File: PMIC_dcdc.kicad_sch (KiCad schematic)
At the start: 21 parts, among them U5 RK809-2

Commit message: updated foorprints
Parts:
- L1, L2, L3, L4: value 470nH 0.035ohm -> 470nH 4.53A 0.035ohm; footprint (none) -> Inductor_SMD:L_1008_2520Metric; LCSC (none) -> C88530; Model (none) -> VLS252010HBX-R47M-1; Vendor (none) -> TDK
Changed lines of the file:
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@@
       (effects (font (size 1.27 1.27)))
     )
-    (property "Value" "470nH 0.035ohm" (at 193.04 96.52 90)
-      (effects (font (size 1.27 1.27)))
-    )
-    (property "Footprint" "" (at 193.04 93.98 0)
+    (property "Value" "470nH 4.53A 0.035ohm" (at 193.04 96.52 90)
+      (effects (font (size 1.27 1.27)))
+    )
+    (property "Footprint" "Inductor_SMD:L_1008_2520Metric" (at 193.04 93.98 0)
       (effects (font (size 1.27 1.27)) hide)
     )
     (property "Datasheet" "~" (at 193.04 93.98 0)
+      (effects (font (size 1.27 1.27)) hide)
+    )
+    (property "Description" "电感值: 470nH 精度: ±20% 额定电流: 3.32A 饱和电流(Isat): 4.53A 直流电阻(DCR): 35mΩ Q值: - 自谐振频率: - 车" (at 193.04 93.98 0)
+      (effects (font (size 1.27 1.27)) hide)
+    )
+    (property "LCSC" "C88530" (at 193.04 93.98 0)
+      (effects (font (size 1.27 1.27)) hide)
+    )
+    (property "Model" "VLS252010HBX-R47M-1" (at 193.04 93.98 0)
+      (effects (font (size 1.27 1.27)) hide)
+    )
+    (property "Vendor" "TDK" (at 193.04 93.98 0)
       (effects (font (size 1.27 1.27)) hide)
     )
@@
       (effects (font (size 1.27 1.27)))
     )
-    (property "Value" "470nH 0.035ohm" (at 194.31 69.85 90)
-      (effects (font (size 1.27 1.27)))
-    )
-    (property "Footprint" "" (at 194.31 67.31 0)
+    (property "Value" "470nH 4.53A 0.035ohm" (at 194.31 69.85 90)
+      (effects (font (size 1.27 1.27)))
+    )
+    (property "Footprint" "Inductor_SMD:L_1008_2520Metric" (at 194.31 67.31 0)
       (effects (font (size 1.27 1.27)) hide)
     )
     (property "Datasheet" "~" (at 194.31 67.31 0)
+      (effects (font (size 1.27 1.27)) hide)
+    )
+    (property "Description" "电感值: 470nH 精度: ±20% 额定电流: 3.32A 饱和电流(Isat): 4.53A 直流电阻(DCR): 35mΩ Q值: - 自谐振频率: - 车" (at 194.31 67.31 0)
+      (effects (font (size 1.27 1.27)) hide)
+    )
+    (property "LCSC" "C88530" (at 194.31 67.31 0)
+      (effects (font (size 1.27 1.27)) hide)
+    )
+    (property "Model" "VLS252010HBX-R47M-1" (at 194.31 67.31 0)
+      (effects (font (size 1.27 1.27)) hide)
+    )
+    (property "Vendor" "TDK" (at 194.31 67.31 0)
       (effects (font (size 1.27 1.27)) hide)
     )
@@
       (effects (font (size 1.27 1.27)))
     )
-    (property "Value" "470nH 0.035ohm" (at 102.87 69.85 90)
-      (effects (font (size 1.27 1.27)))
-    )
-    (property "Footprint" "" (at 102.87 67.31 0)
+    (property "Value" "470nH 4.53A 0.035ohm" (at 102.87 69.85 90)
+      (effects (font (size 1.27 1.27)))
+    )
+    (property "Footprint" "Inductor_SMD:L_1008_2520Metric" (at 102.87 67.31 0)
       (effects (font (size 1.27 1.27)) hide)
     )
@@
       (effects (font (size 1.27 1.27)) hide)
     )
+    (property "Description" "电感值: 470nH 精度: ±20% 额定电流: 3.32A 饱和电流(Isat): 4.53A 直流电阻(DCR): 35mΩ Q值: - 自谐振频率: - 车" (at 102.87 67.31 0)
+      (effects (font (size 1.27 1.27)) hide)
+    )
+    (property "LCSC" "C88530" (at 102.87 67.31 0)
+      (effects (font (size 1.27 1.27)) hide)
+    )
+    (property "Model" "VLS252010HBX-R47M-1" (at 102.87 67.31 0)
+      (effects (font (size 1.27 1.27)) hide)
+    )
+    (property "Vendor" "TDK" (at 102.87 67.31 0)
+      (effects (font (size 1.27 1.27)) hide)
+    )
     (pin "1")
     (pin "2")
@@
       (effects (font (size 1.27 1.27)))
     )
-    (property "Value" "470nH 0.035ohm" (at 104.14 107.95 90)
-      (effects (font (size 1.27 1.27)))
-    )
-    (property "Footprint" "" (at 104.14 105.41 0)
+    (property "Value" "470nH 4.53A 0.035ohm" (at 104.14 107.95 90)
+      (effects (font (size 1.27 1.27)))
+    )
+    (property "Footprint" "Inductor_SMD:L_1008_2520Metric" (at 104.14 105.41 0)
       (effects (font (size 1.27 1.27)) hide)
     )
@@
       (effects (font (size 1.27 1.27)) hide)
     )
+    (property "Description" "电感值: 470nH 精度: ±20% 额定电流: 3.32A 饱和电流(Isat): 4.53A 直流电阻(DCR): 35mΩ Q值: - 自谐振频率: - 车" (at 104.14 105.41 0)
+      (effects (font (size 1.27 1.27)) hide)
+    )
+    (property "LCSC" "C88530" (at 104.14 105.41 0)
+      (effects (font (size 1.27 1.27)) hide)
+    )
+    (property "Model" "VLS252010HBX-R47M-1" (at 104.14 105.41 0)
+      (effects (font (size 1.27 1.27)) hide)
+    )
+    (property "Vendor" "TDK" (at 104.14 105.41 0)
+      (effects (font (size 1.27 1.27)) hide)
+    )

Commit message: fix some ERCs
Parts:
- renumbered C50 to C64, C51 to C65, C52 to C66, C53 to C67, C54 to C68, C55 to C69, C56 to C70, C57 to C71, C58 to C72, C59 to C73, C60 to C74, C61 to C75, R47 to R43, R48 to R44, R49 to R45, R50 to R46, U5 to U4
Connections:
- net VDD_DDR renamed VCC_DDR
- net VDD_NPU_VEPU renamed VDD_NPU

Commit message: added VDD Logic
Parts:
- R43, R44: LCSC (none) -> C25138; Model (none) -> 0402WGJ0101TCE; Vendor (none) -> UNI-ROYAL(厚声)
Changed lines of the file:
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@@
+      (effects (font (size 1.27 1.27)) hide)
+    )
+    (property "Description" "电阻类型: 厚膜电阻 阻值: 100Ω 精度: ±5% 功率: 1/16W 温度系数: ±100ppm/℃ 最大工作电压: 50V 工作温度" (at 102.87 76.2 0)
+      (effects (font (size 1.27 1.27)) hide)
+    )
+    (property "LCSC" "C25138" (at 102.87 76.2 0)
+      (effects (font (size 1.27 1.27)) hide)
+    )
+    (property "Model" "0402WGJ0101TCE" (at 102.87 76.2 0)
+      (effects (font (size 1.27 1.27)) hide)
+    )
+    (property "Vendor" "UNI-ROYAL(厚声)" (at 102.87 76.2 0)
       (effects (font (size 1.27 1.27)) hide)
     )
@@
       (effects (font (size 1.27 1.27)) hide)
     )
+    (property "Description" "电阻类型: 厚膜电阻 阻值: 100Ω 精度: ±5% 功率: 1/16W 温度系数: ±100ppm/℃ 最大工作电压: 50V 工作温度" (at 104.14 114.3 0)
+      (effects (font (size 1.27 1.27)) hide)
+    )
+    (property "LCSC" "C25138" (at 104.14 114.3 0)
+      (effects (font (size 1.27 1.27)) hide)
+    )
+    (property "Model" "0402WGJ0101TCE" (at 104.14 114.3 0)
+      (effects (font (size 1.27 1.27)) hide)
+    )
+    (property "Vendor" "UNI-ROYAL(厚声)" (at 104.14 114.3 0)
+      (effects (font (size 1.27 1.27)) hide)
+    )

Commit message: updated for ERC
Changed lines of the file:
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@@
-    (stroke (width 0) (type default))
-  )
-  (wire (pts (xy 232.41 113.03) (xy 232.41 114.3))
     (stroke (width 0) (type default))
   )
@@
         )
       )
-    )
-  )
-  (symbol (lib_id "power:PWR_FLAG") (at 232.41 113.03 0) (unit 1)
-    (in_bom yes) (on_board yes) (dnp no) (fields_autoplaced)
-    (property "Reference" "#FLG011" (at 232.41 111.125 0)
-      (effects (font (size 1.27 1.27)) hide)
-    )
-    (property "Value" "PWR_FLAG" (at 232.41 109.5281 0)
-      (effects (font (size 1.27 1.27)))
-    )
-    (property "Footprint" "" (at 232.41 113.03 0)
-      (effects (font (size 1.27 1.27)) hide)
-    )
-    (property "Datasheet" "~" (at 232.41 113.03 0)
-      (effects (font (size 1.27 1.27)) hide)
-    )
-    (pin "1")
-    (instances
-      (project "leaf"
-        (path "/e3b58043-16a3-43c8-9fad-9c9784eebfa4/cc9fb3ac-19c3-47a8-ba7d-678b4d514ff0/46e9a7bf-8506-4399-90d8-57d007223126/2d95e8c5-bd08-40b5-b7b2-fac89748aabf"
-          (reference "#FLG011") (unit 1)
-        )
-      )

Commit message: added OSC, updated annotations
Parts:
- renumbered C64 to C14001, C65 to C14002, C66 to C14003, C67 to C14004, C68 to C14005, C69 to C14006, C70 to C14007, C71 to C14008, C72 to C14009, C73 to C14010, C74 to C14011, C75 to C14012, L1 to L14001, L2 to L14002, L3 to L14003, L4 to L14004, R43 to R14001, R44 to R14002, R45 to R14003, R46 to R14004, U4 to U13001

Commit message: move DDR power decoupling capacitors into DDR4 Sheet
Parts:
- renumbered C14001 to C68, C14002 to C69, C14003 to C70, C14004 to C71, C14005 to C72, C14006 to C73, C14007 to C74, C14008 to C75, C14009 to C76, C14010 to C77, C14011 to C78, C14012 to C79, L14001 to L2, L14002 to L3, L14003 to L4, L14004 to L5, R14001 to R43, R14002 to R44, R14003 to R45, R14004 to R46, U13001 to U5

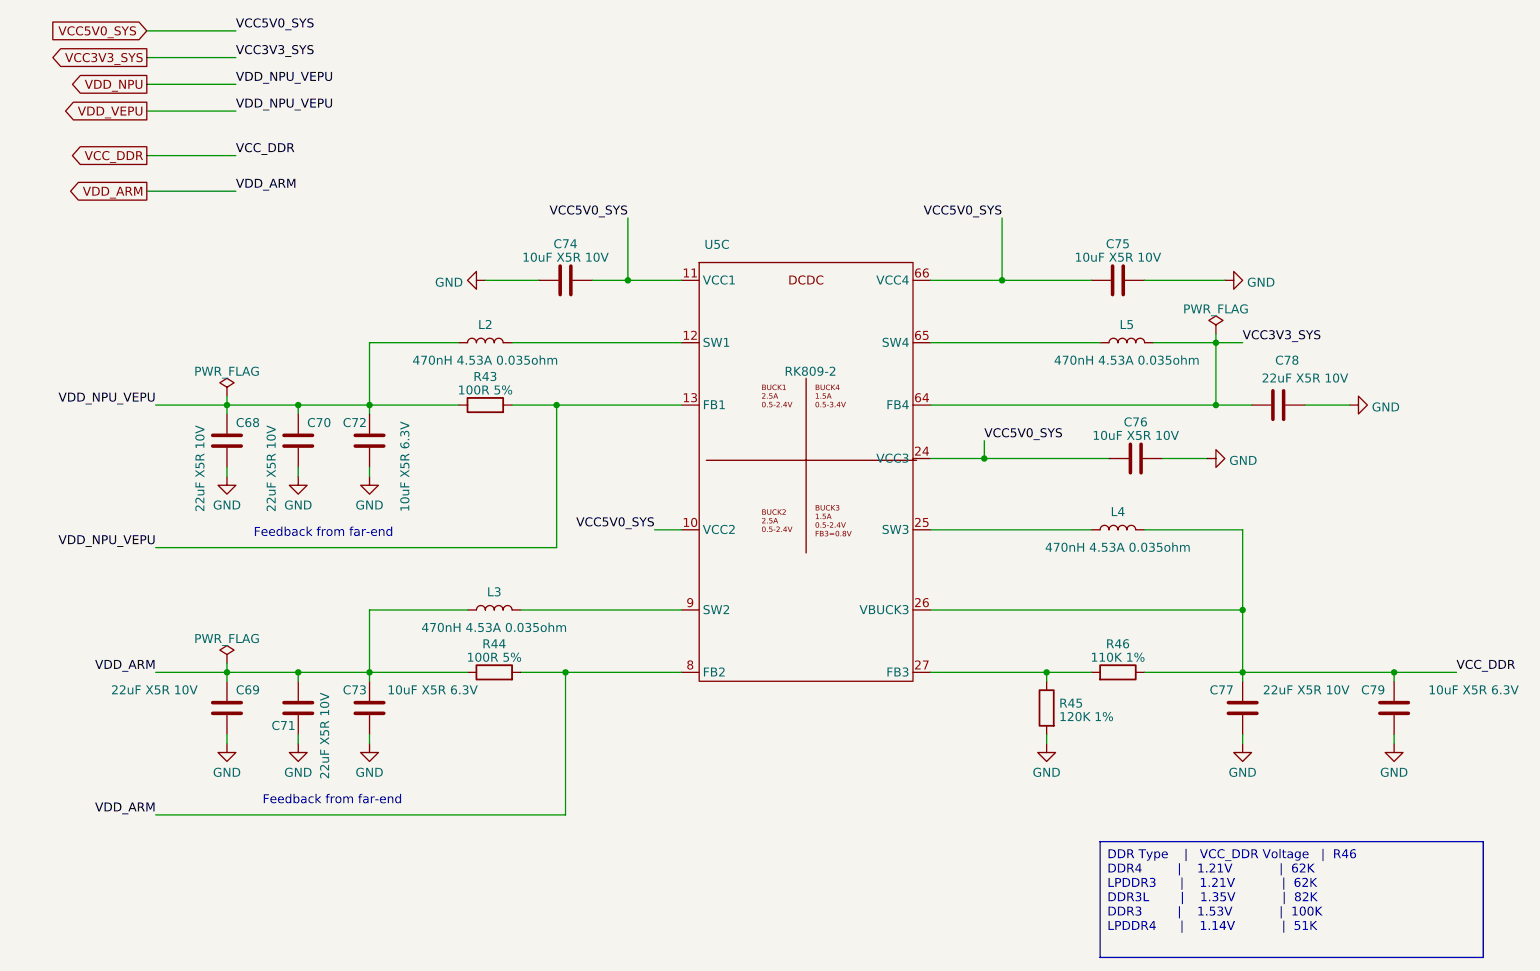
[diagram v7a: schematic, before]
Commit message: resort all symbols
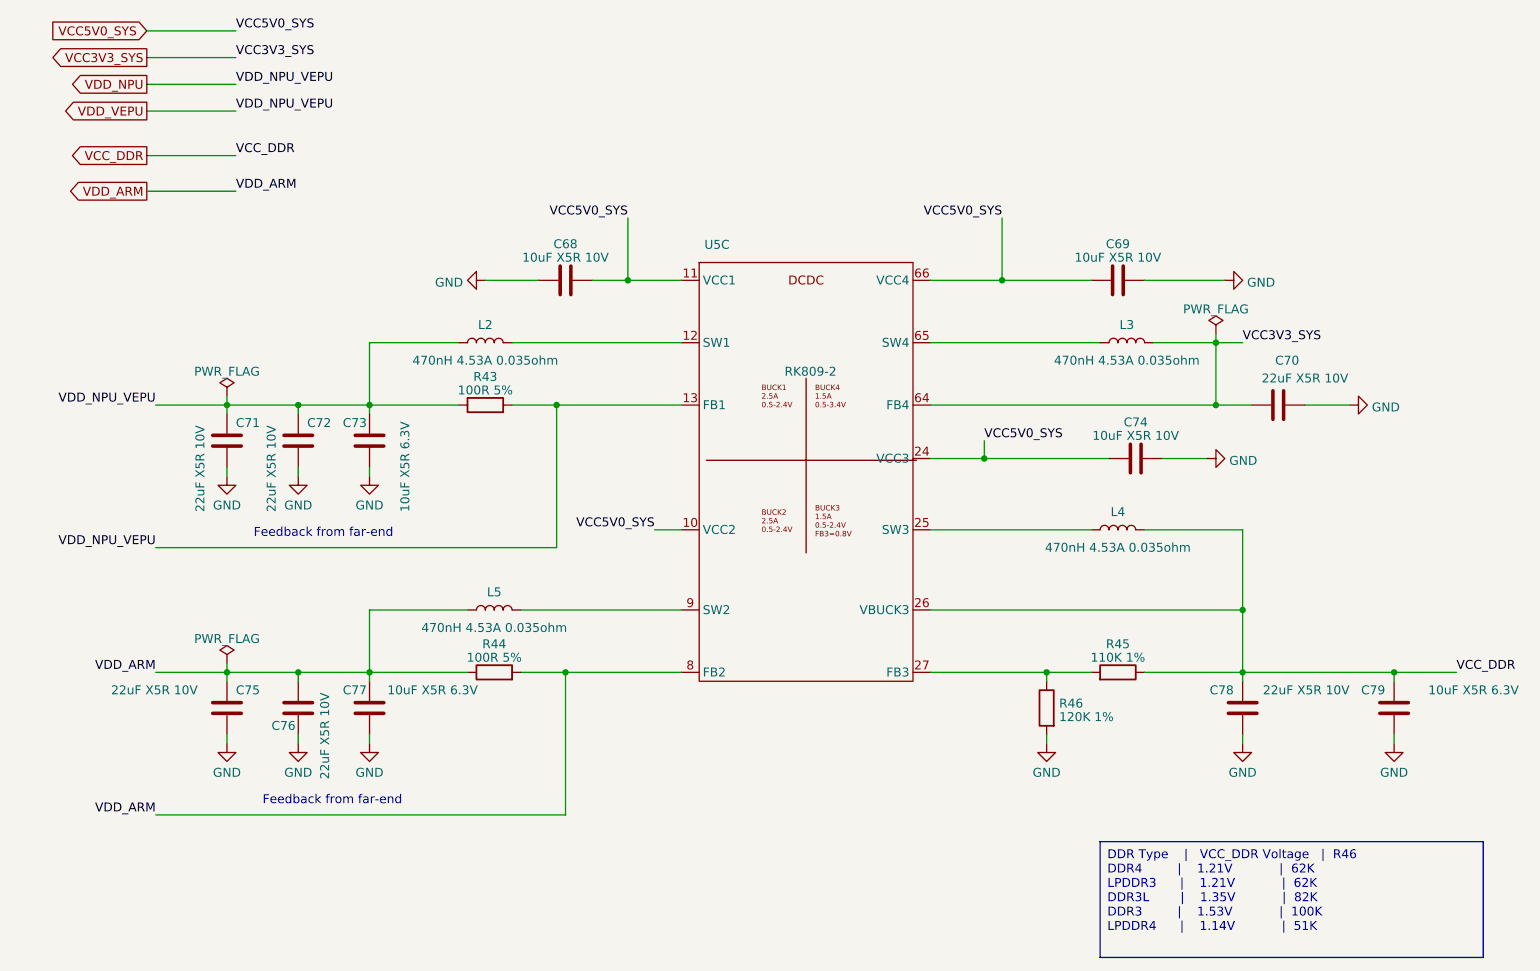
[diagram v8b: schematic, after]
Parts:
- renumbered C74 to C68, C75 to C69, C78 to C70, C68 to C71, C70 to C72, C72 to C73, C76 to C74, C69 to C75, C71 to C76, C73 to C77, C77 to C78, L5 to L3, L3 to L5, R46 to R45, R45 to R46
